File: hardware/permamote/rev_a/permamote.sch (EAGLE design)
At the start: 98 parts, among them J1 TC2030-JLINK-NL, J2 M10X2, J3 M04X2, J5 MICRO_USB_B_HIROSE_ZX62R-B-5P, Q1 PMDXB950UPEL, Q10 PMDXB950UPEL, Q2 PMDXB950UPEL, Q3 PMDXB950UPEL, Q4 PMDXB950UPEL, Q5 PMDXB950UPEL, Q6 PMDXB950UPEL, Q7 PMDXB950UPEL, Q8 PMDXB950UPEL, U1 AB1815-T3, U10 NRF52840, U11 SI7021-A20-GM1, U12 FT232RQ, U2 BQ25505, U3 EKMB1101111, U4 ISL29125, U5 LIS2DW12, U6 MAX17222, U7 MAX44009, U8 MS5637-02BA03, X1 32MHz, X3 32.768kHz, X4 ABS07-32.768KHZ-7-T

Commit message: WIP reroute signals
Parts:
- C17: device passives:CAPACITOR0603_CAP -> passives:CAPACITOR0402_CAP
- C8: device passives:CAPACITOR0402_CAP -> passives:CAPACITOR0603_CAP
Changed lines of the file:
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@@
 <part name="P+19" library="mote" deviceset="VSW" device=""/>
 <part name="GND20" library="supply1" library_urn="urn:adsk.eagle:library:371" deviceset="GND" device=""/>
-<part name="C17" library="passives" deviceset="CAPACITOR" device="0603_CAP" value="10nF">
+<part name="C17" library="passives" deviceset="CAPACITOR" device="0402_CAP" value="10nF">
 <attribute name="DIGIKEY" value="490-4516-1-ND"/>
 </part>
@@
 <attribute name="DIGIKEY" value="445-5947-1-ND"/>
 </part>
-<part name="C8" library="passives" deviceset="CAPACITOR" device="0402_CAP" value="4.7uF">
+<part name="C8" library="passives" deviceset="CAPACITOR" device="0603_CAP" value="4.7uF">
 <attribute name="DIGIKEY" value="445-5947-1-ND"/>
 </part>

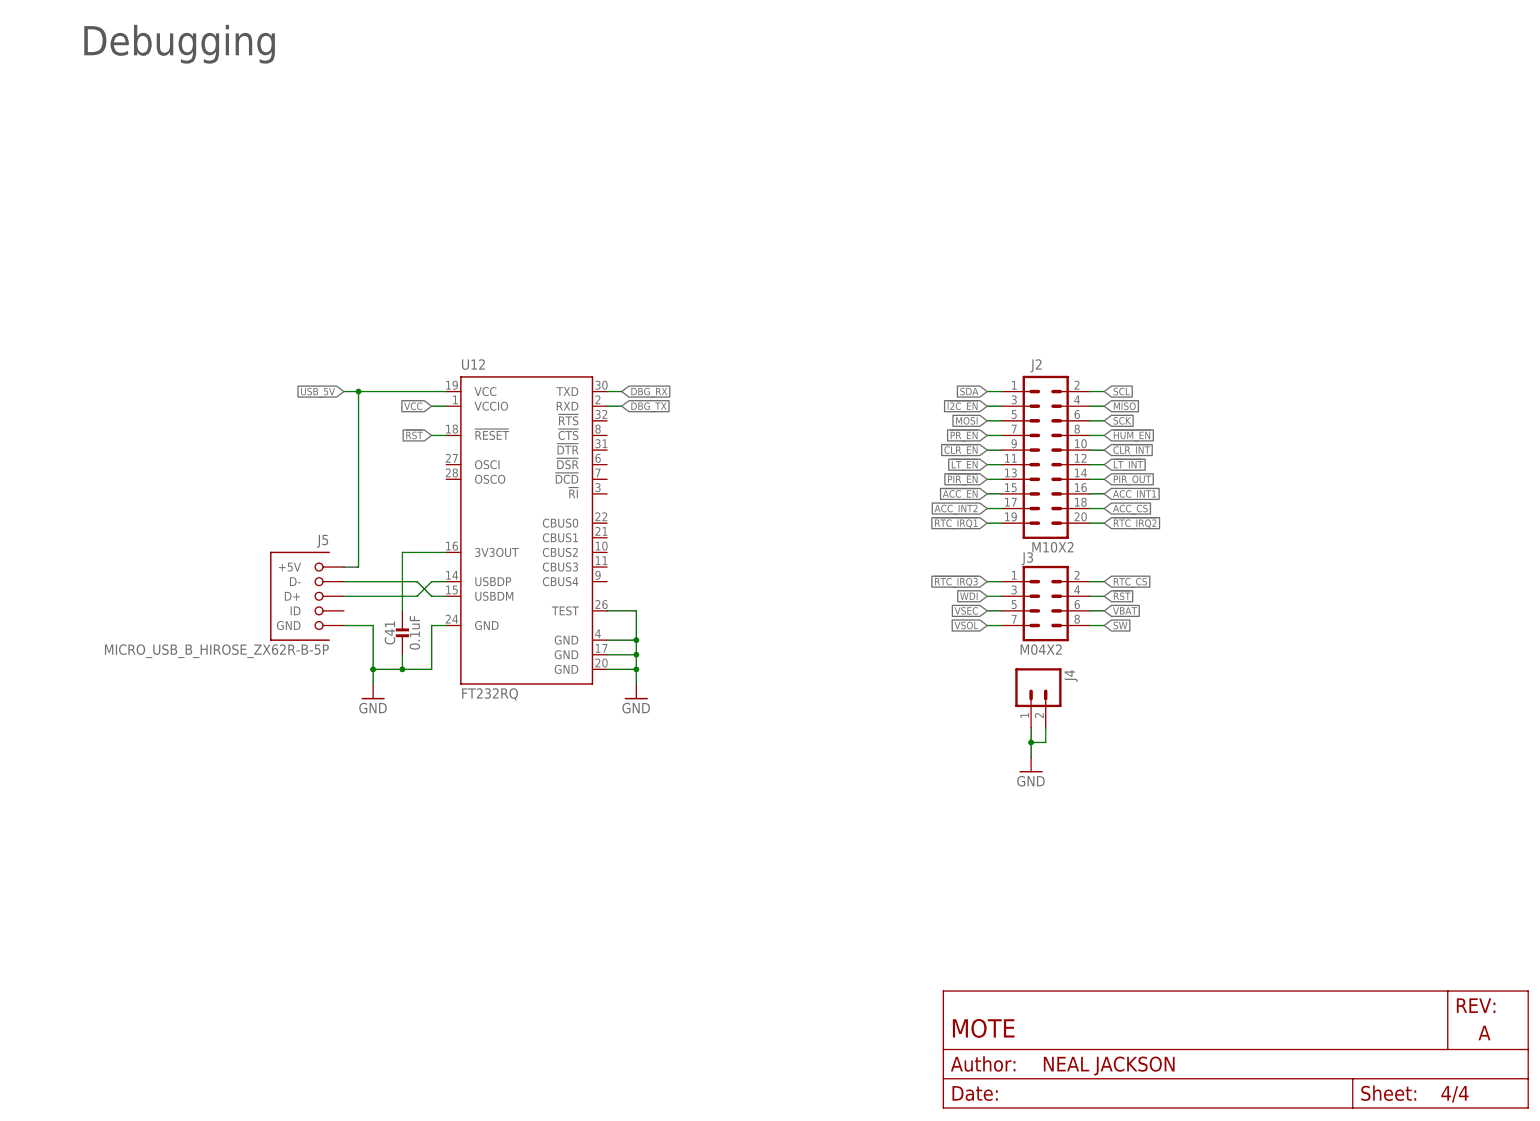
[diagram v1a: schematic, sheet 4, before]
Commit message: No airwires
Add testpoints, connect dbg uart tx/rx lines
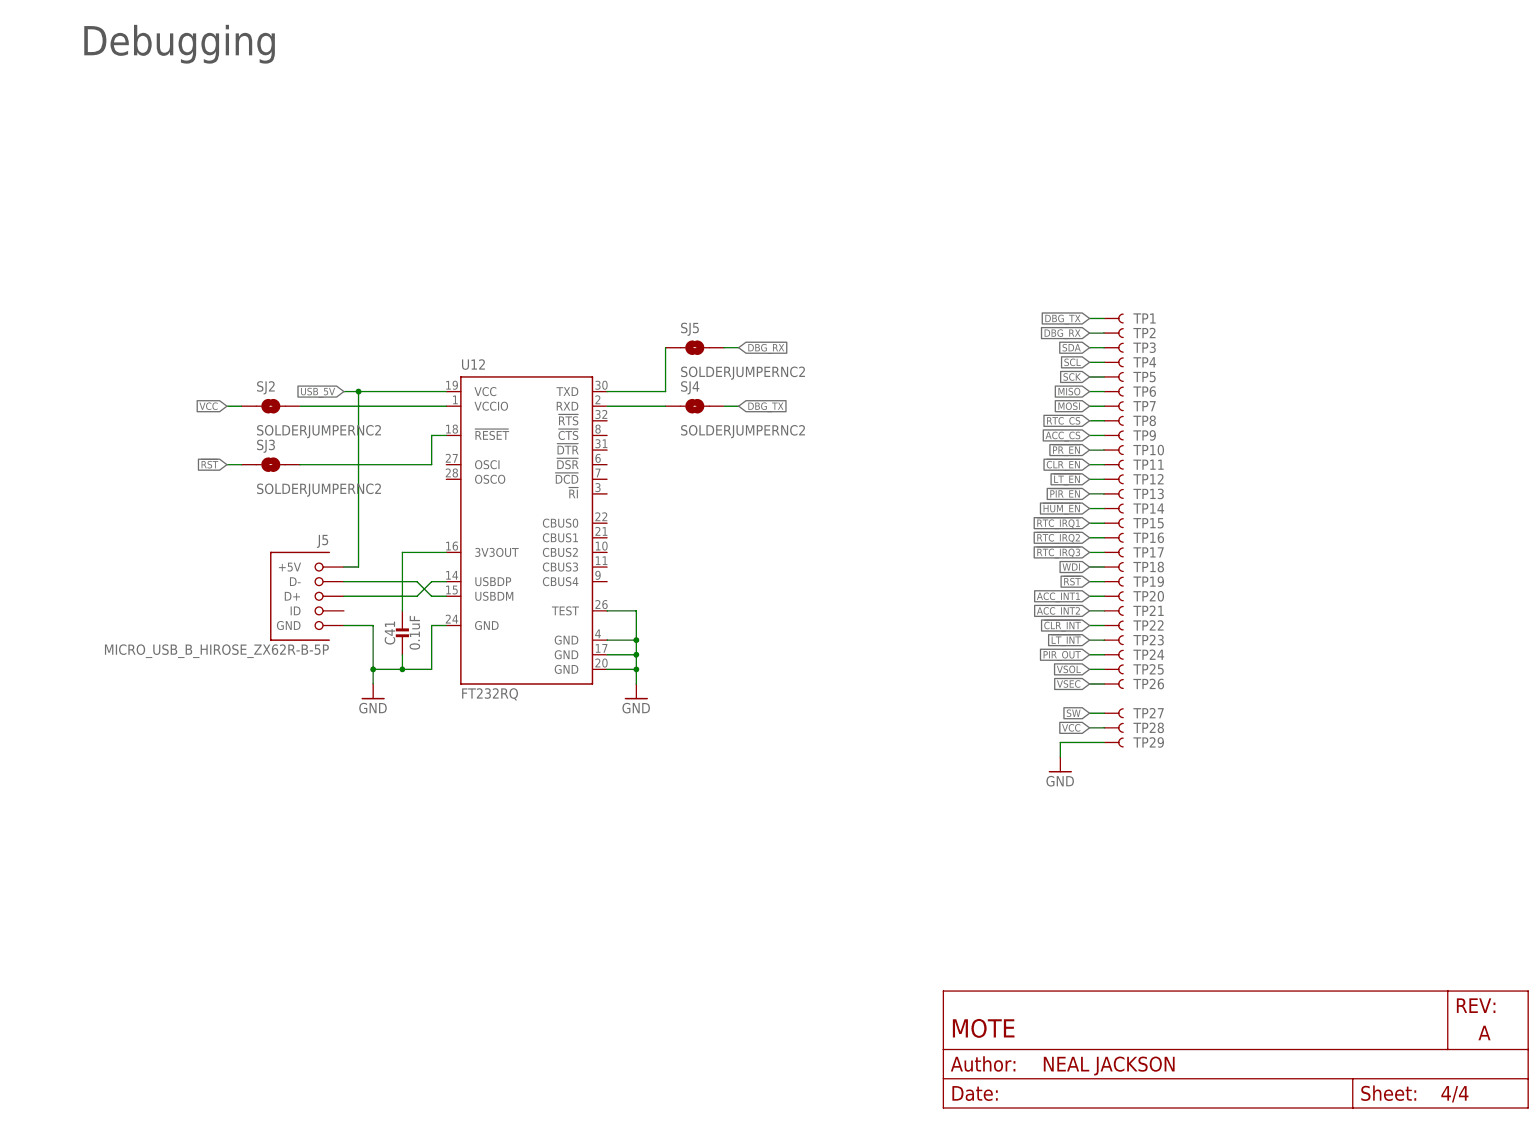
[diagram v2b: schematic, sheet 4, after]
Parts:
- removed J2: M10X2, SparkFun-Connectors:M10X2
- removed J3: M04X2, SparkFun-Connectors:M04X2
- removed J4: (no value), SparkFun-Connectors:M02PTH
- added SJ2, SJ3, SJ4, SJ5: SOLDERJUMPERNC2, SparkFun-Passives:SOLDERJUMPERNC2
- added TP1, TP10, TP11, TP12, TP13, TP14, TP15, TP16, TP17, TP18, TP19, TP2, TP20, TP21, TP22, TP23, TP24, TP25, TP26, TP27, TP28, TP29, TP3, TP4, TP5, TP6, TP7, TP8, TP9: TEST-POINT3, headers:TEST-POINT3
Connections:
- removed net !ACC_EN: J2.15
- removed net !I2C_EN: J2.3
- new net !FTDI_RESET: SJ3.2, U12.!RESET
- new net FTDI_VCCIO: SJ2.2, U12.VCCIO
- new net RXD: SJ4.1, U12.RXD
- new net TXD: SJ5.1, U12.TXD
- net !CLR_EN: now also TP11.1, U10.P0.25; no longer J2.9, U10.P0.11
- net !CLR_INT: now also TP22.1, U10.P0.23; no longer J2.10, U10.P1.02
- net !HUM_EN: now also TP14.1, U10.P1.08; no longer J2.8, U10.P0.12
- net !LT_EN: now also TP12.1, U10.P0.20; no longer J2.11, U10.P1.13
- net !LT_INT: now also TP23.1, U10.P0.22; no longer J2.12, U10.P1.04
- net !PIR_EN: now also TP13.1, U10.P1.01; no longer J2.13, U10.P1.10
- net !PR_EN: now also TP10.1, U10.P0.11; no longer J2.7, U10.P1.11
- net !RST: now also SJ3.1, TP19.1; no longer J3.4, U10.P0.17, U12.!RESET
- net !RTC_IRQ1: now also TP15.1, U10.P0.16; no longer J2.19, U10.P0.14
- net !RTC_IRQ2: now also TP16.1, U10.P0.19; no longer J2.20, U10.P0.20
- net !RTC_IRQ3: now also TP17.1, U10.P0.17; no longer J3.1, U10.P1.07
- net ACC_CS: now also TP9.1, U10.P0.07; no longer J2.18, U10.P0.13
- net ACC_INT1: now also TP20.1, U10.P0.06; no longer J2.16, U10.P1.06
- net ACC_INT2: now also TP21.1, U10.P0.05/AIN3; no longer J2.17, U10.P0.09/NFC1
- net DBG_RX: now also SJ5.2, TP2.1, U10.P0.26; no longer U12.TXD
- net DBG_TX: now also SJ4.2, TP1.1, U10.P0.27; no longer U12.RXD
- net GND: now also TP29.1; no longer J4.1, J4.2
- net MISO: now also TP6.1, U10.P0.12; no longer J2.4, U10.P1.00
- net MOSI: now also TP7.1, U10.P0.08; no longer J2.5, U10.P0.24
- net PIR_OUT: now also TP24.1, U10.P1.03; no longer J2.14, U10.P1.01
- net RTC_CS: now also TP8.1, U10.P0.14; no longer J3.2, U10.P0.15
- net SCK: now also TP5.1, U10.P1.09; no longer J2.6, U10.P0.22
- net SCL: now also TP4.1, U10.P0.24; no longer J2.2, U10.P0.08
- net SDA: now also TP3.1, U10.P1.00; no longer J2.1, U10.P0.06
- net SW: now also TP27.1, U10.P0.28/AIN4; no longer J3.8, U10.P0.26
- net VBAT: no longer J3.6, U10.P0.04/AIN2
- net VCC: now also SJ2.1, TP28.1; no longer U12.VCCIO
- net VSEC: now also TP26.1, U10.P0.04/AIN2; no longer J3.5, U10.P0.02/AIN0
- net VSOL: now also TP25.1, U10.P0.30/AIN6; no longer J3.7, U10.P0.29/AIN5
- net WDI: now also TP18.1, U10.P0.15; no longer J3.3, U10.P0.31/AIN7
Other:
- note removed: "AD12 is in the way of the actual Reset pin, AC13, so we just route over it."

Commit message: rearrange board
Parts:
- removed TP10, TP11, TP12, TP13, TP14, TP15, TP16, TP17, TP18, TP19, TP2, TP20, TP21, TP22, TP23, TP24, TP25, TP26, TP27, TP28, TP29, TP3, TP4, TP5, TP6, TP7, TP8, TP9: TEST-POINT3, headers:TEST-POINT3
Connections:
- net !CLR_EN: no longer TP11.1
- net !CLR_INT: no longer TP22.1
- net !HUM_EN: no longer TP14.1
- net !LT_EN: no longer TP12.1
- net !LT_INT: no longer TP23.1
- net !PIR_EN: no longer TP13.1
- net !PR_EN: no longer TP10.1
- net !RST: no longer TP19.1
- net !RTC_IRQ1: no longer TP15.1
- net !RTC_IRQ2: no longer TP16.1
- net !RTC_IRQ3: no longer TP17.1
- net ACC_CS: no longer TP9.1
- net ACC_INT1: no longer TP20.1
- net ACC_INT2: no longer TP21.1
- net DBG_RX: no longer TP2.1
- net GND: no longer TP29.1
- net MISO: no longer TP6.1
- net MOSI: no longer TP7.1
- net PIR_OUT: no longer TP24.1
- net RTC_CS: no longer TP8.1
- net SCK: no longer TP5.1
- net SCL: no longer TP4.1
- net SDA: no longer TP3.1
- net SW: no longer TP27.1
- net VCC: no longer TP28.1
- net VSEC: no longer TP26.1
- net VSOL: no longer TP25.1
- net WDI: no longer TP18.1

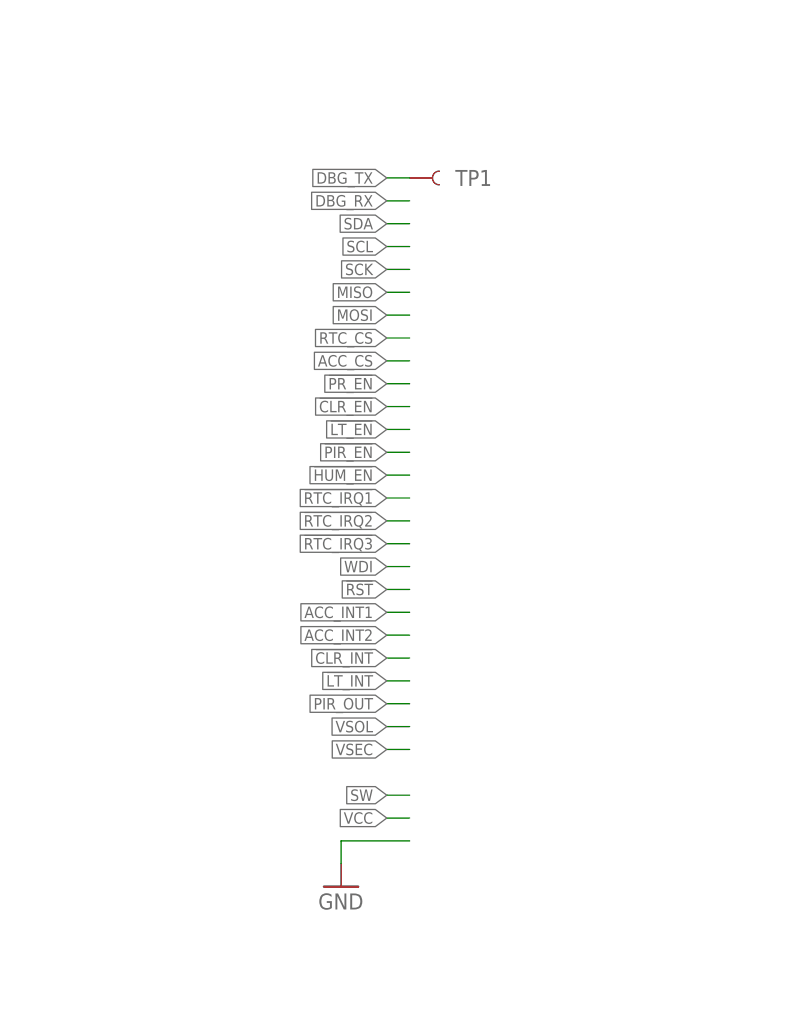
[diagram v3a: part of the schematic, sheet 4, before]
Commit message: Rearrange board to move light sensors to bottom edge
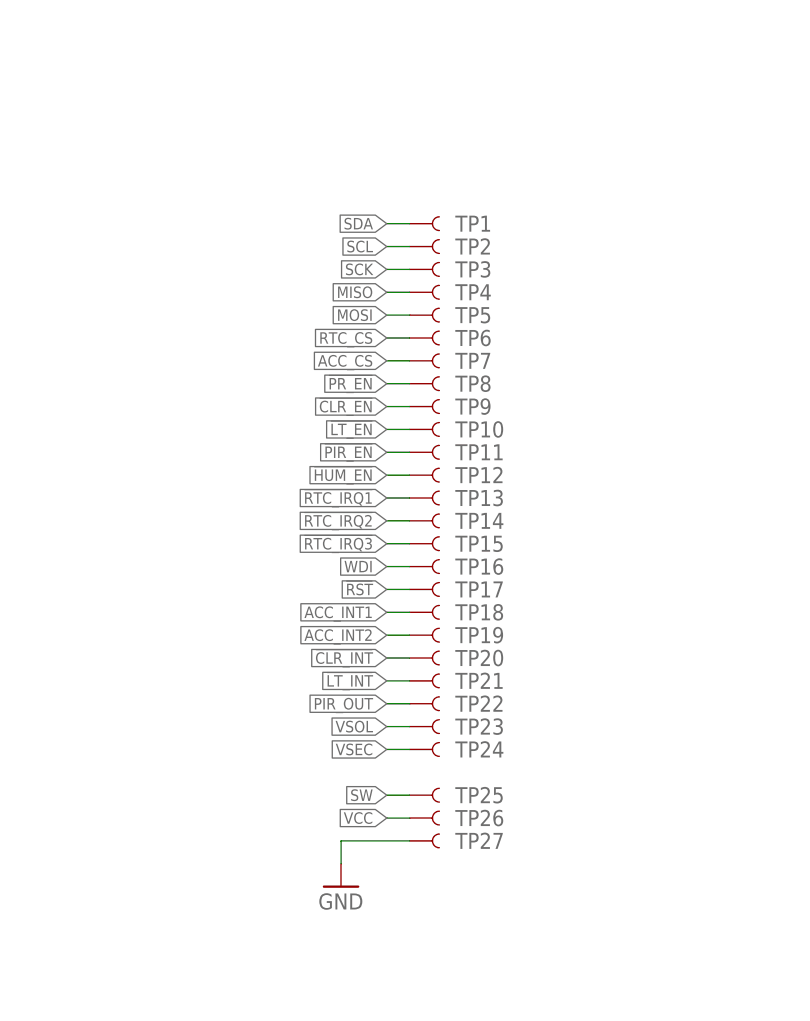
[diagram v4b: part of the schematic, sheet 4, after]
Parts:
- added TP10, TP11, TP12, TP13, TP14, TP15, TP16, TP17, TP18, TP19, TP2, TP20, TP21, TP22, TP23, TP24, TP25, TP26, TP27, TP3, TP4, TP5, TP6, TP7, TP8, TP9: TEST-POINT3, headers:TEST-POINT3
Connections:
- net !CLR_EN: now also TP9.1
- net !CLR_INT: now also TP20.1
- net !HUM_EN: now also TP12.1, U10.P1.10; no longer U10.P1.08
- net !LT_EN: now also TP10.1, U10.P0.24; no longer U10.P0.20
- net !LT_INT: now also TP21.1, U10.P1.00; no longer U10.P0.22
- net !PIR_EN: now also TP11.1, U10.P0.17; no longer U10.P1.01
- net !PR_EN: now also TP8.1, U10.P1.11; no longer U10.P0.11
- net !RST: now also TP17.1
- net !RTC_IRQ1: now also TP13.1, U10.P1.13; no longer U10.P0.16
- net !RTC_IRQ2: now also TP14.1, U10.P1.14; no longer U10.P0.19
- net !RTC_IRQ3: now also TP15.1, U10.P1.15; no longer U10.P0.17
- net ACC_CS: now also TP7.1, U10.P0.21; no longer U10.P0.07
- net ACC_INT1: now also TP18.1, U10.P0.20; no longer U10.P0.06
- net ACC_INT2: now also TP19.1, U10.P0.22; no longer U10.P0.05/AIN3
- net DBG_TX: no longer TP1.1
- net GND: now also TP27.1
- net MISO: now also TP4.1, U10.P1.09; no longer U10.P0.12
- net MOSI: now also TP5.1
- net PIR_OUT: now also TP22.1, U10.P0.16; no longer U10.P1.03
- net RTC_CS: now also TP6.1, U10.P1.12; no longer U10.P0.14
- net SCK: now also TP3.1, U10.P0.12; no longer U10.P1.09
- net SCL: now also TP2.1, U10.P0.14; no longer U10.P0.24
- net SDA: now also TP1.1, U10.P0.15; no longer U10.P1.00
- net SW: now also TP25.1
- net VBAT: now also U10.P0.29/AIN5
- net VCC: now also TP26.1
- net VSEC: now also TP24.1, U10.P0.31/AIN7; no longer U10.P0.04/AIN2
- net VSOL: now also TP23.1
- net WDI: now also TP16.1, U10.P0.02/AIN0; no longer U10.P0.15
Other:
- moved on the sheet: TP1

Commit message: Add Debug LED
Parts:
- added D2: SML-LX0404SIUPGUSB, leds:SML-LX0404SIUPGUSB
- added R17, R18, R8: 470, passives:RESISTOR0402_RES
- D1: value SOLARCELL -> SOLARCELLHOLES; device mote:SOLARCELL -> permamote:SOLARCELLHOLES
- TP1, TP10, TP11, TP12, TP13, TP14, TP15, TP16, TP17, TP18, TP19, TP2, TP20, TP21, TP22, TP23, TP24, TP25, TP26, TP27, TP3, TP4, TP5, TP6, TP7, TP8, TP9: value TEST-POINT3 -> TEST-POINT; device headers:TEST-POINT3 -> headers:TEST-POINT
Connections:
- new net LED_BLUE: R18.2, U10.P0.05/AIN3
- new net LED_GREEN: R17.2, U10.P0.06
- new net LED_RED: R8.2, U10.P0.04/AIN2
- new net N$15: D2.R, R8.1
- new net N$17: D2.G, R17.1
- new net N$19: D2.B, R18.1
- net !CLR_EN: now also TP9.TESTPOINT; no longer TP9.1
- net !CLR_INT: now also TP20.TESTPOINT; no longer TP20.1
- net !HUM_EN: now also TP12.TESTPOINT; no longer TP12.1
- net !LT_EN: now also TP10.TESTPOINT; no longer TP10.1
- net !LT_INT: now also TP21.TESTPOINT; no longer TP21.1
- net !PIR_EN: now also TP11.TESTPOINT; no longer TP11.1
- net !PR_EN: now also TP8.TESTPOINT; no longer TP8.1
- net !RST: now also TP17.TESTPOINT; no longer TP17.1
- net !RTC_IRQ1: now also TP13.TESTPOINT; no longer TP13.1
- net !RTC_IRQ2: now also TP14.TESTPOINT; no longer TP14.1
- net !RTC_IRQ3: now also TP15.TESTPOINT; no longer TP15.1
- net ACC_CS: now also TP7.TESTPOINT; no longer TP7.1
- net ACC_INT1: now also TP18.TESTPOINT; no longer TP18.1
- net ACC_INT2: now also TP19.TESTPOINT; no longer TP19.1
- net GND: now also TP27.TESTPOINT; no longer TP27.1
- net MISO: now also TP4.TESTPOINT; no longer TP4.1
- net MOSI: now also TP5.TESTPOINT; no longer TP5.1
- net PIR_OUT: now also TP22.TESTPOINT; no longer TP22.1
- net RTC_CS: now also TP6.TESTPOINT; no longer TP6.1
- net SCK: now also TP3.TESTPOINT; no longer TP3.1
- net SCL: now also TP2.TESTPOINT; no longer TP2.1
- net SDA: now also TP1.TESTPOINT; no longer TP1.1
- net SW: now also TP25.TESTPOINT; no longer TP25.1
- net VCC: now also D2.VDD, TP26.TESTPOINT; no longer TP26.1
- net VSEC: now also TP24.TESTPOINT; no longer TP24.1
- net VSOL: now also TP23.TESTPOINT; no longer TP23.1
- net WDI: now also TP16.TESTPOINT; no longer TP16.1
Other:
- moved on the sheet: TP1, TP10, TP11, TP12, TP13, TP14, TP15, TP16, TP17, TP18, TP19, TP2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
